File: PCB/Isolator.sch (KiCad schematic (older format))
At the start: 1 part, among them U2 LM358

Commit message: Libraries and footprints adjustments. New connectors (4 pins main, 2 pins debug and 6 pins isp). New source input cap.
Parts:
- U2: symbol LM358-RESCUE-ArduBooster -> LM358
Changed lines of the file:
@@
 EESchema Schematic File Version 2
-LIBS:ArduBooster-rescue
 LIBS:power
 LIBS:device
@@
 Rev "1.0"
 Comp ""
-Comment1 ""
+Comment1 "Used to isolate DAC to output"
 Comment2 ""
 Comment3 ""
@@
 $EndDescr
 $Comp
-L LM358-RESCUE-ArduBooster U2
+L LM358 U2
 U 1 1 54D7D0D1
 P 5650 2800
@@
 $EndComp
 Wire Wire Line
-	5150 2900 5050 2900
+	5050 2900 5350 2900
 Wire Wire Line
 	5050 2900 5050 3300
@@
 	6250 3300 6250 2800
 Wire Wire Line
-	5550 3500 5550 3200
+	5550 3100 5550 3500
 Wire Wire Line
-	5550 2150 5550 2400
+	5550 2150 5550 2500
 $Comp
-L LM358-RESCUE-ArduBooster U2
+L LM358 U2
 U 2 1 54D7D175
 P 5650 4800
@@
 $EndComp
 Wire Wire Line
-	5550 5500 5550 5200
+	5550 5100 5550 5500
 Wire Wire Line
-	5150 4900 5050 4900
+	5050 4900 5350 4900
 Wire Wire Line
 	5050 4900 5050 5300
@@
 	6250 5300 6250 4800
 Wire Wire Line
-	6150 4800 6500 4800
+	5950 4800 6500 4800
 Wire Wire Line
-	5550 4200 5550 4400
+	5550 4200 5550 4500
 Wire Wire Line
-	4400 2700 5150 2700
+	4400 2700 5350 2700
 Connection ~ 6250 2800
 Connection ~ 6250 4800
 Wire Wire Line
-	6150 2800 6500 2800
+	5950 2800 6500 2800
 Wire Wire Line
-	5150 4700 4400 4700
+	4400 4700 5350 4700
 Text HLabel 5550 2150 1    60   Output ~ 0
 +9V

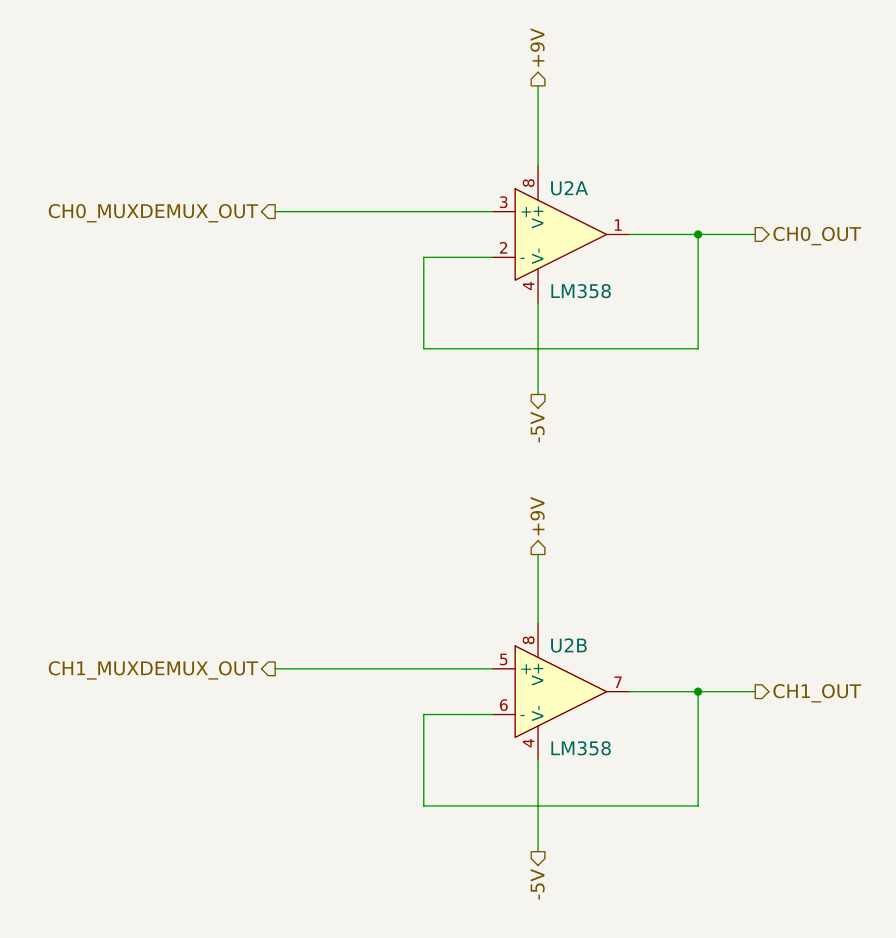
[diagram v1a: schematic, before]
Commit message: New connectors connection. Labels corrections (direction).
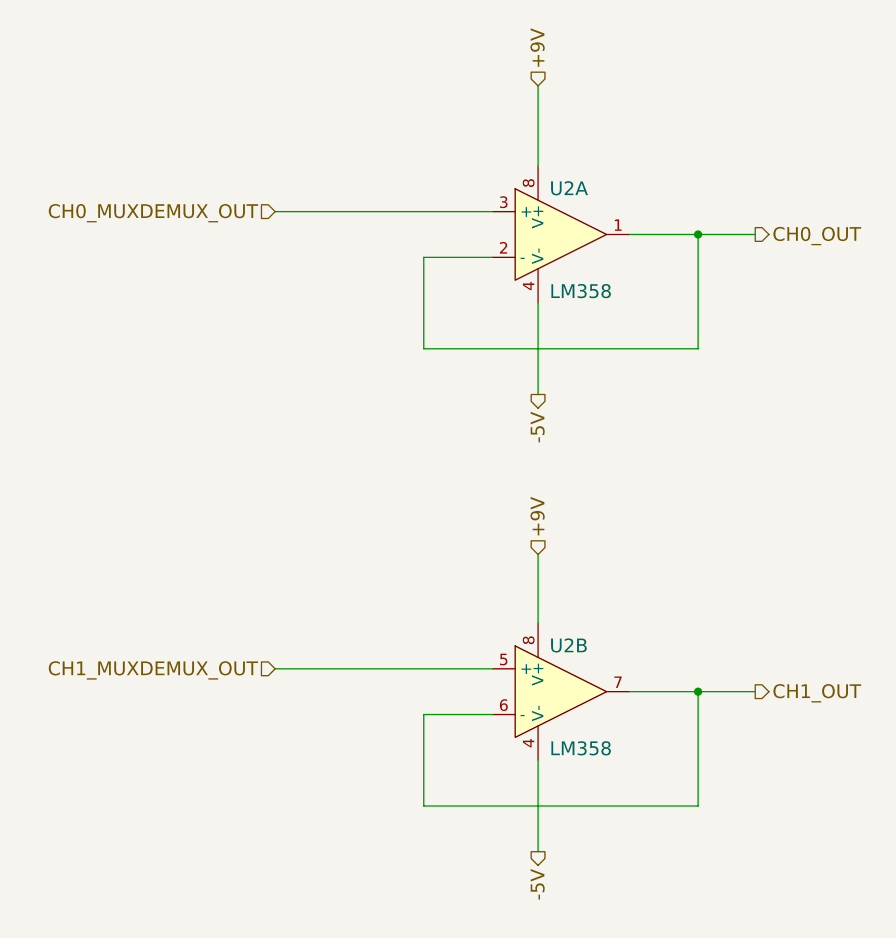
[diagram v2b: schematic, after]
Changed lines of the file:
@@
 Wire Wire Line
 	4400 4700 5350 4700
-Text HLabel 5550 2150 1    60   Output ~ 0
+Text HLabel 5550 2150 1    60   Input ~ 0
 +9V
 Text HLabel 6500 2800 2    60   Output ~ 0
@@
 Text HLabel 5550 3500 3    60   Output ~ 0
 -5V
-Text HLabel 4400 2700 0    60   Output ~ 0
+Text HLabel 4400 2700 0    60   Input ~ 0
 CH0_MUXDEMUX_OUT
-Text HLabel 4400 4700 0    60   Output ~ 0
+Text HLabel 4400 4700 0    60   Input ~ 0
 CH1_MUXDEMUX_OUT
-Text HLabel 5550 4200 1    60   Output ~ 0
+Text HLabel 5550 4200 1    60   Input ~ 0
 +9V
 Text HLabel 6500 4800 2    60   Output ~ 0

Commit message: Correct DIP sockets footprints.
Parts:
- U2: footprint Sockets_DIP:DIP-8__300 -> Housings_DIP:DIP-8_W7.62mm_LongPads
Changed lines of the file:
@@
 F 0 "U2" H 5600 3000 60  0000 L CNN
 F 1 "LM358" H 5600 2550 60  0000 L CNN
-F 2 "Sockets_DIP:DIP-8__300" H 5650 2800 60  0001 C CNN
+F 2 "Housings_DIP:DIP-8_W7.62mm_LongPads" H 5650 2800 60  0001 C CNN
 F 3 "" H 5650 2800 60  0000 C CNN
 	1    5650 2800
@@
 F 0 "U2" H 5600 5000 60  0000 L CNN
 F 1 "LM358" H 5600 4550 60  0000 L CNN
-F 2 "Sockets_DIP:DIP-8__300" H 5650 4800 60  0001 C CNN
+F 2 "Housings_DIP:DIP-8_W7.62mm_LongPads" H 5650 4800 60  0001 C CNN
 F 3 "" H 5650 4800 60  0000 C CNN
 	2    5650 4800
